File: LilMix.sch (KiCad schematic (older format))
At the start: 57 parts, among them J1_L1 MONO, J1_R1 MONO, J2_L1 MONO, J2_R1 MONO, J3 STEREO, J4 MONO, J5 MONO, J6 STEREO, U1 TL074, U2 NE5532

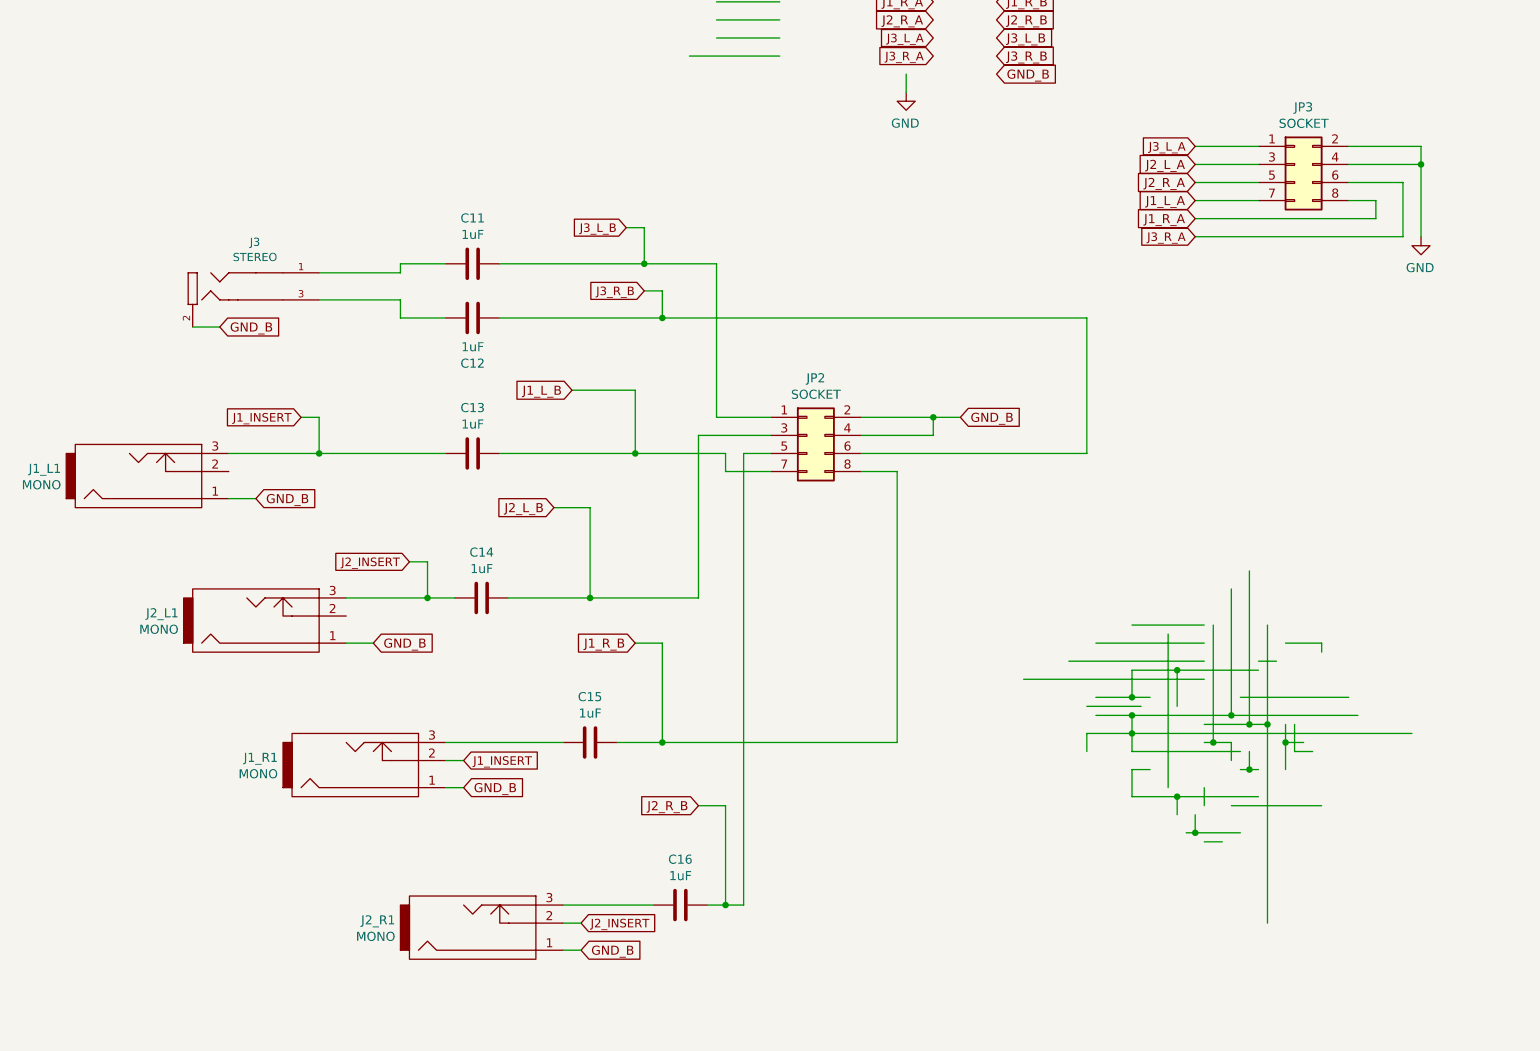
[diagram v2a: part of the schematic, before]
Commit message: Removed extra jack connection from schematic. Added second jack to 3rd channel. Repositioned jack board for even space between jacks, with slightly reduced overall dimensions
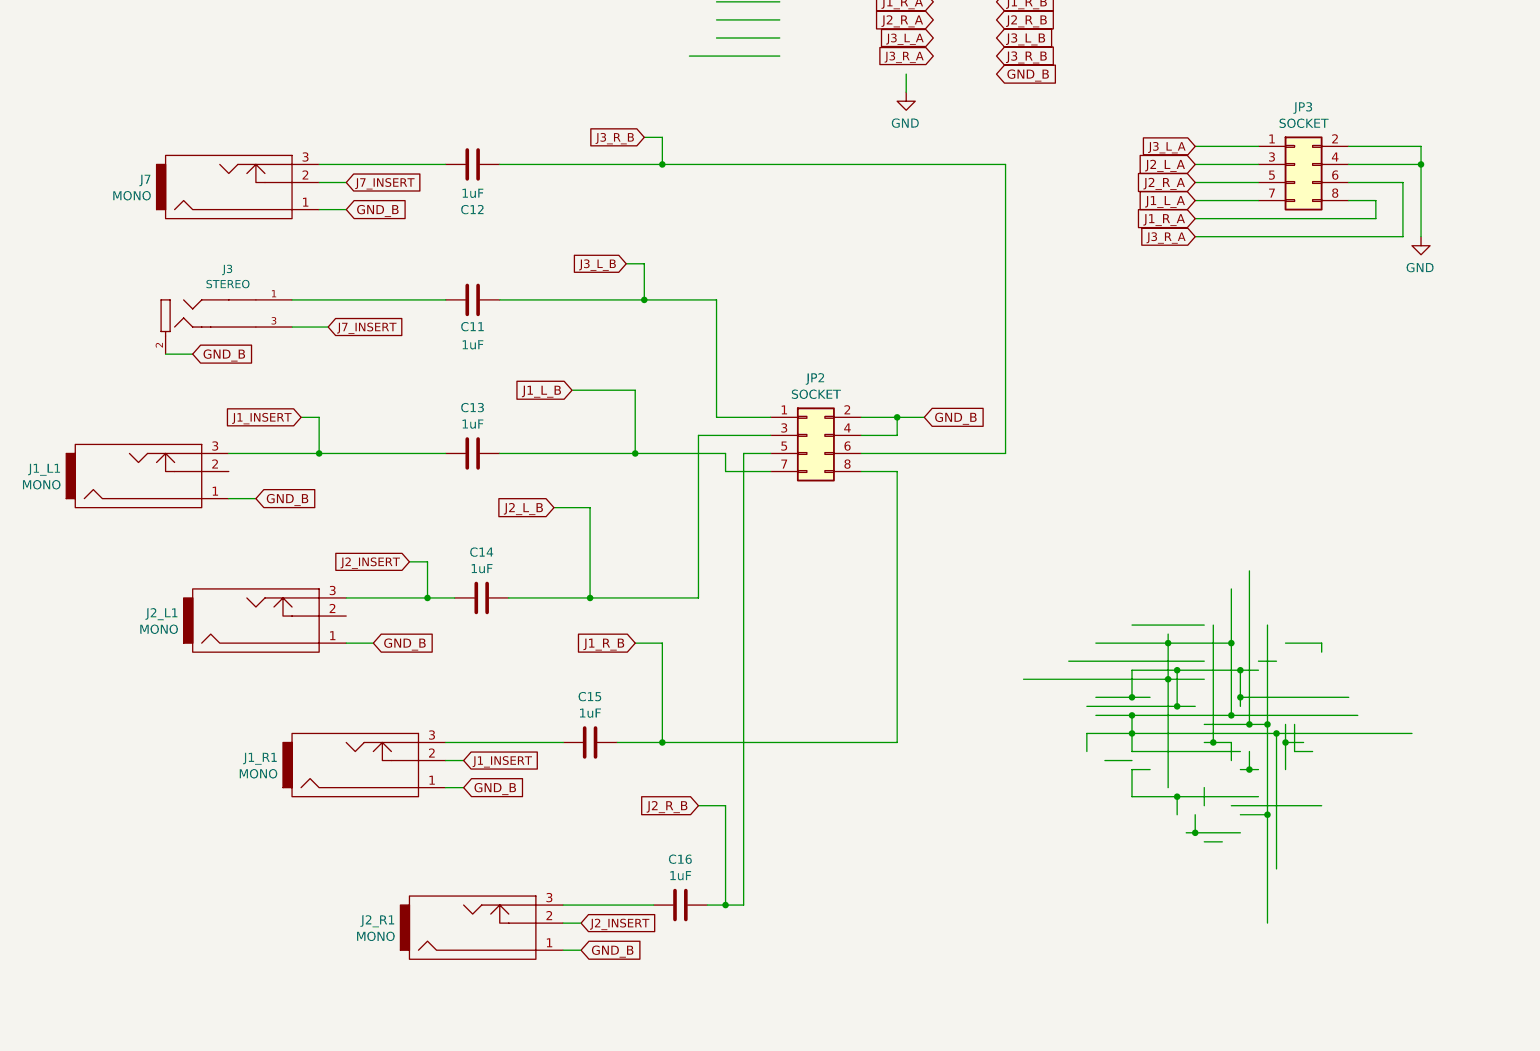
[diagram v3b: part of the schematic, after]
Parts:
- added J7: MONO, 4ms-footprints:PJ301M-12, symbol eurocad:PJ301M-12
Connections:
- net labels added: J7_INSERT
- wire segments 313 -> 326
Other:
- moved on the sheet: C11, C12, J3
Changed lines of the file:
@@
 EESchema Schematic File Version 4
-LIBS:LilMix-cache
 EELAYER 30 0
 EELAYER END
@@
 L 4ms-mech:JACK-STEREO-MINI J3
 U 1 1 5ECFAA7B
-P -6850 2450
-F 0 "J3" H -6905 2720 45  0000 C CNN
-F 1 "STEREO" H -6905 2636 45  0000 C CNN
-F 2 "Eurocad:STPX-3501-3C-1" H -6820 2600 20  0001 C CNN
-F 3 "" H -6850 2450 60  0001 C CNN
-	1    -6850 2450
+P -7000 2600
+F 0 "J3" H -7055 2870 45  0000 C CNN
+F 1 "STEREO" H -7055 2786 45  0000 C CNN
+F 2 "Eurocad:STPX-3501-3C-1" H -6970 2750 20  0001 C CNN
+F 3 "" H -7000 2600 60  0001 C CNN
+	1    -7000 2600
 	1    0    0    -1
 $EndComp
@@
 $EndComp
 Wire Wire Line
-	-4750 2100 -4850 2100
+	-4750 2300 -4850 2300
 Wire Wire Line
 	-5850 5050 -5750 5050
@@
 	0    1    -1   0
 $EndComp
-Text GLabel -4850 2100 0    47   Input ~ 0
+Text GLabel -4850 2300 0    47   Input ~ 0
 J3_L_B
 Text GLabel -5100 5950 2    47   Input ~ 0
@@
 	1000 2200 1450 2200
 Wire Wire Line
-	-2650 4600 -1650 4600
+	-2650 4600 -1850 4600
 Wire Wire Line
 	-6400 4400 -6250 4400
@@
 J2_R_B
 Wire Wire Line
-	-1850 4350 -1850 5200
-Wire Wire Line
-	-4650 2450 -4750 2450
-Text GLabel -4750 2450 0    47   Input ~ 0
+	-1850 4350 -1850 4400
+Wire Wire Line
+	-4650 1600 -4750 1600
+Text GLabel -4750 1600 0    47   Input ~ 0
 J3_R_B
 Text GLabel -2800 750  2    50   Input ~ 0
@@
 Wire Wire Line
 	1000 6000 1450 6000
-Text GLabel -3000 3150 2    50   Input ~ 0
+Text GLabel -3200 3150 2    50   Input ~ 0
 GND_B
 Wire Wire Line
-	-3150 3150 -3000 3150
+	-3350 3150 -3200 3150
 Text Notes -4050 7400 0    354  ~ 0
 LilMix External
@@
 Wire Wire Line
 	-2050 4300 -1650 4300
-Wire Wire Line
-	-1650 4400 -2250 4400
-Text GLabel -7100 2650 2    50   Input ~ 0
+Text GLabel -7250 2800 2    50   Input ~ 0
 GND_B
 Wire Wire Line
-	-7250 2650 -7100 2650
-Wire Wire Line
-	-3550 3250 -3150 3250
-Wire Wire Line
-	-3550 3150 -3150 3150
-Wire Wire Line
-	-3150 3150 -3150 3250
+	-7400 2800 -7250 2800
+Wire Wire Line
+	-3550 3250 -3350 3250
+Wire Wire Line
+	-3550 3150 -3350 3150
+Wire Wire Line
+	-3350 3150 -3350 3250
 Wire Wire Line
 	-7050 3350 -6550 3350
@@
 	1    0    0    -1
 $EndComp
-Connection ~ -3150 3150
+Connection ~ -3350 3150
 $Comp
 L 4ms-headers:Conn_02x04_Odd_Even JP3
@@
 L 4ms-passives:C C11
 U 1 1 5E6EE0E9
-P -5700 2300
-F 0 "C11" V -5952 2300 50  0000 C CNN
-F 1 "1uF" V -5861 2300 50  0000 C CNN
-F 2 "Capacitor_THT:C_Rect_L7.0mm_W4.5mm_P5.00mm" H -5662 2150 50  0001 C CNN
-F 3 "" H -5700 2300 50  0001 C CNN
-	1    -5700 2300
-	0    1    1    0
-$EndComp
-Wire Wire Line
-	-4650 2450 -4650 2600
+P -5700 2500
+F 0 "C11" V -5550 2500 50  0000 C CNN
+F 1 "1uF" V -5450 2500 50  0000 C CNN
+F 2 "Capacitor_THT:C_Rect_L7.0mm_W4.5mm_P5.00mm" H -5662 2350 50  0001 C CNN
+F 3 "" H -5700 2500 50  0001 C CNN
+	1    -5700 2500
+	0    1    1    0
+$EndComp
+Wire Wire Line
+	-4650 1600 -4650 1750
 $Comp
 L 4ms-passives:C C12
 U 1 1 5E77E136
-P -5700 2600
-F 0 "C12" V -5952 2600 50  0000 C CNN
-F 1 "1uF" V -5861 2600 50  0000 C CNN
-F 2 "Capacitor_THT:C_Rect_L7.0mm_W4.5mm_P5.00mm" H -5662 2450 50  0001 C CNN
-F 3 "" H -5700 2600 50  0001 C CNN
-	1    -5700 2600
+P -5700 1750
+F 0 "C12" V -5952 1750 50  0000 C CNN
+F 1 "1uF" V -5861 1750 50  0000 C CNN
+F 2 "Capacitor_THT:C_Rect_L7.0mm_W4.5mm_P5.00mm" H -5662 1600 50  0001 C CNN
+F 3 "" H -5700 1750 50  0001 C CNN
+	1    -5700 1750
 	0    -1   -1   0
 $EndComp
 Wire Wire Line
-	-6550 2350 -6100 2350
-Wire Wire Line
-	-6100 2350 -6100 2300
-Wire Wire Line
-	-6100 2300 -5850 2300
-Wire Wire Line
-	-5550 2300 -4750 2300
-Wire Wire Line
-	-4750 2300 -4750 2100
-Wire Wire Line
-	-2000 4750 -2300 4750
+	-5550 2500 -4750 2500
+Wire Wire Line
+	-4750 2500 -4750 2300
 Wire Wire Line
 	-1400 4000 -1400 4850
 Wire Wire Line
-	-6550 2500 -6100 2500
-Wire Wire Line
-	-6100 2500 -6100 2600
-Wire Wire Line
-	-6100 2600 -5850 2600
-Wire Wire Line
-	-5550 2600 -4650 2600
+	-5550 1750 -4650 1750
 Wire Wire Line
 	-1600 4300 -1600 4950
@@
 	-4050 3450 -4300 3450
 Wire Wire Line
-	-1500 4100 -1500 4800
+	-1500 4100 -1500 4400
 Wire Wire Line
 	-2250 4700 -2050 4700
@@
 	-4200 5850 -4300 5850
 Connection ~ -4300 5850
-Wire Wire Line
-	-4800 3350 -4300 3350
 Wire Wire Line
 	-4300 3350 -4300 3450
@@
 Connection ~ -5050 4150
 Wire Wire Line
-	-4650 2600 -2300 2600
-Wire Wire Line
-	-2300 2600 -2300 3350
-Wire Wire Line
-	-2300 3350 -3550 3350
-Connection ~ -4650 2600
+	-4650 1750 -2750 1750
+Wire Wire Line
+	-1250 4900 -1250 5650
+Connection ~ -4650 1750
 Wire Wire Line
 	-4050 3150 -4350 3150
 Wire Wire Line
-	-4350 3150 -4350 2300
-Wire Wire Line
-	-4350 2300 -4750 2300
-Connection ~ -4750 2300
+	-1850 4600 -1850 4400
+Wire Wire Line
+	-4350 2500 -4750 2500
+Connection ~ -4750 2500
 Connection ~ -2050 4700
 Connection ~ -2050 4800
 Connection ~ -1800 4550
 Wire Wire Line
-	-1800 4550 -1350 4550
+	-1800 4550 -1450 4550
 Wire Wire Line
 	-1450 4700 -850 4700
@@
 	-1400 5100 -1350 5100
 Wire Wire Line
-	-2050 4900 -500 4900
+	-2050 4900 -1250 4900
 Wire Wire Line
 	-2050 4800 -1500 4800
@@
 	-1000 4400 -1000 4450
 Wire Wire Line
-	-1300 4850 -1300 5950
+	-1300 4850 -1300 5350
 Connection ~ -1700 5450
 Wire Wire Line
@@
 Wire Wire Line
 	-1800 5250 -1350 5250
+$Comp
+L eurocad:PJ301M-12 J7
+U 1 1 5E5614B6
+P -7000 1850
+F 0 "J7" H -7478 1834 50  0000 R CNN
+F 1 "MONO" H -7478 1925 50  0000 R CNN
+F 2 "4ms-footprints:PJ301M-12" H -7000 1850 50  0001 C CNN
+F 3 "" H -7000 1850 50  0000 C CNN
+	1    -7000 1850
+	1    0    0    1
+$EndComp
+Wire Wire Line
+	-2750 3350 -2750 1750
+Wire Wire Line
+	-2050 5050 -2200 5050
+Connection ~ -1500 4400
+Connection ~ -1250 4900
+Wire Wire Line
+	-1250 4900 -500 4900
+Wire Wire Line
+	-2250 4400 -1850 4400
+Text GLabel -6400 1850 2    47   Input ~ 0
+J7_INSERT
+Wire Wire Line
+	-1450 4550 -1450 4700
+Wire Wire Line
+	-4350 3150 -4350 2500
+Connection ~ -1450 4550
+Wire Wire Line
+	-1450 4550 -1350 4550
+Connection ~ -1450 4700
+Wire Wire Line
+	-1450 4700 -1450 4750
+Wire Wire Line
+	-6700 2500 -5850 2500
+Wire Wire Line
+	-6550 1850 -6400 1850
+Text GLabel -6500 2650 2    47   Input ~ 0
+J7_INSERT
+Wire Wire Line
+	-6700 2650 -6500 2650
+Wire Wire Line
+	-6550 1750 -5850 1750
+Connection ~ -1800 4750
+Wire Wire Line
+	-1800 4750 -1700 4750
+Wire Wire Line
+	-2300 4750 -1800 4750
+Wire Wire Line
+	-1500 4400 -1500 4800
+Wire Wire Line
+	-1450 5350 -1300 5350
+Wire Wire Line
+	-2750 3350 -3550 3350
+Connection ~ -1300 5350
+Wire Wire Line
+	-1300 5350 -1300 5950
+Text GLabel -6400 2000 2    50   Input ~ 0
+GND_B
+Wire Wire Line
+	-6550 2000 -6400 2000
+Connection ~ -1850 4400
+Wire Wire Line
+	-1850 4400 -1500 4400
+Connection ~ -1850 4600
+Wire Wire Line
+	-1850 4600 -1650 4600
+Wire Wire Line
+	-1850 4600 -1850 5200
+Wire Wire Line
+	-4800 3350 -4300 3350
 $EndSCHEMATC

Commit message: Fixed J7 insert
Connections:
- wire segments 326 -> 325
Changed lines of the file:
@@
 J2_INSERT
 Wire Wire Line
-	-6550 3150 -6550 3350
-Wire Wire Line
-	-6650 3150 -6550 3150
-Text GLabel -6650 3150 0    47   Input ~ 0
+	-6900 3450 -7050 3450
+Text GLabel -6900 3450 2    47   Input ~ 0
 J1_INSERT
 Wire Wire Line
@@
 Wire Wire Line
 	-3350 3150 -3350 3250
-Wire Wire Line
-	-7050 3350 -6550 3350
 $Comp
 L 4ms-headers:Conn_02x04_Odd_Even JP2
@@
 Wire Wire Line
 	-4800 3350 -5550 3350
-Wire Wire Line
-	-5850 3350 -6550 3350
-Connection ~ -6550 3350
 $Comp
 L 4ms-passives:C C14
@@
 	-1400 5100 -1350 5100
 Wire Wire Line
-	-2050 4900 -1250 4900
-Wire Wire Line
 	-2050 4800 -1500 4800
 Wire Wire Line
@@
 	-1850 4600 -1650 4600
 Wire Wire Line
+	-4800 3350 -4300 3350
+Wire Wire Line
+	-7050 3350 -5850 3350
+Wire Wire Line
 	-1850 4600 -1850 5200
 Wire Wire Line
-	-4800 3350 -4300 3350
+	-2050 4900 -1250 4900
+Wire Wire Line
+	-1750 4950 -1750 5150
 $EndSCHEMATC

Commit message: Change TL074 output channel feedback resistors, based on BB results
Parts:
- R11, R12, R15, R16: value 10k -> 100k
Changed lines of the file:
@@
 P 7550 1150
 F 0 "R15" V 7650 1150 50  0000 C CNN
-F 1 "10k" V 7434 1150 50  0000 C CNN
+F 1 "100k" V 7434 1150 50  0000 C CNN
 F 2 "Resistor_SMD:R_0805_2012Metric_Pad1.15x1.40mm_HandSolder" V 7480 1150 50  0001 C CNN
 F 3 "" H 7550 1150 50  0001 C CNN
@@
 P 7550 2750
 F 0 "R16" V 7650 2750 50  0000 C CNN
-F 1 "10k" V 7434 2750 50  0000 C CNN
+F 1 "100k" V 7434 2750 50  0000 C CNN
 F 2 "Resistor_SMD:R_0805_2012Metric_Pad1.15x1.40mm_HandSolder" V 7480 2750 50  0001 C CNN
 F 3 "" H 7550 2750 50  0001 C CNN
@@
 P 6900 3100
 F 0 "R12" V 7000 3100 50  0000 C CNN
-F 1 "10k" V 6784 3100 50  0000 C CNN
+F 1 "100k" V 6784 3100 50  0000 C CNN
 F 2 "Resistor_SMD:R_0805_2012Metric_Pad1.15x1.40mm_HandSolder" V 6830 3100 50  0001 C CNN
 F 3 "" H 6900 3100 50  0001 C CNN
@@
 P 6900 1500
 F 0 "R11" V 7000 1500 50  0000 C CNN
-F 1 "10k" V 6784 1500 50  0000 C CNN
+F 1 "100k" V 6784 1500 50  0000 C CNN
 F 2 "Resistor_SMD:R_0805_2012Metric_Pad1.15x1.40mm_HandSolder" V 6830 1500 50  0001 C CNN
 F 3 "" H 6900 1500 50  0001 C CNN

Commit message: Fix J1 insert from T rather than S
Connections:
- wire segments 325 -> 327
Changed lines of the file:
@@
 J2_INSERT
 Wire Wire Line
-	-6900 3450 -7050 3450
-Text GLabel -6900 3450 2    47   Input ~ 0
+	-6300 3150 -6150 3150
+Text GLabel -6300 3150 0    47   Input ~ 0
 J1_INSERT
 Wire Wire Line
@@
 Wire Wire Line
 	-1800 5250 -1350 5250
+Wire Wire Line
+	-2750 3350 -2750 1750
+Wire Wire Line
+	-2050 5050 -2200 5050
+Connection ~ -1500 4400
+Connection ~ -1250 4900
+Wire Wire Line
+	-1250 4900 -500 4900
+Wire Wire Line
+	-2250 4400 -1850 4400
+Wire Wire Line
+	-1450 4550 -1450 4700
+Wire Wire Line
+	-4350 3150 -4350 2500
+Connection ~ -1450 4550
+Wire Wire Line
+	-1450 4550 -1350 4550
+Connection ~ -1450 4700
+Wire Wire Line
+	-1450 4700 -1450 4750
+Wire Wire Line
+	-6700 2500 -5850 2500
+Connection ~ -1800 4750
+Wire Wire Line
+	-1800 4750 -1700 4750
+Wire Wire Line
+	-2300 4750 -1800 4750
+Wire Wire Line
+	-1500 4400 -1500 4800
+Wire Wire Line
+	-1450 5350 -1300 5350
+Wire Wire Line
+	-2750 3350 -3550 3350
+Connection ~ -1300 5350
+Wire Wire Line
+	-1300 5350 -1300 5950
+Connection ~ -1850 4400
+Wire Wire Line
+	-1850 4400 -1500 4400
+Connection ~ -1850 4600
+Wire Wire Line
+	-1850 4600 -1650 4600
+Wire Wire Line
+	-4800 3350 -4300 3350
+Wire Wire Line
+	-7050 3350 -6150 3350
+Wire Wire Line
+	-1850 4600 -1850 5200
+Wire Wire Line
+	-2050 4900 -1250 4900
+Wire Wire Line
+	-1750 4950 -1750 5150
+Wire Wire Line
+	-6700 2650 -6500 2650
+Text GLabel -6500 2650 2    47   Input ~ 0
+J7_INSERT
+Wire Wire Line
+	-6550 2000 -6400 2000
+Text GLabel -6400 2000 2    50   Input ~ 0
+GND_B
+Wire Wire Line
+	-6550 1750 -5850 1750
+Wire Wire Line
+	-6550 1850 -6400 1850
+Text GLabel -6400 1850 2    47   Input ~ 0
+J7_INSERT
 $Comp
 L eurocad:PJ301M-12 J7
@@
 $EndComp
 Wire Wire Line
-	-2750 3350 -2750 1750
-Wire Wire Line
-	-2050 5050 -2200 5050
-Connection ~ -1500 4400
-Connection ~ -1250 4900
-Wire Wire Line
-	-1250 4900 -500 4900
-Wire Wire Line
-	-2250 4400 -1850 4400
-Text GLabel -6400 1850 2    47   Input ~ 0
-J7_INSERT
-Wire Wire Line
-	-1450 4550 -1450 4700
-Wire Wire Line
-	-4350 3150 -4350 2500
-Connection ~ -1450 4550
-Wire Wire Line
-	-1450 4550 -1350 4550
-Connection ~ -1450 4700
-Wire Wire Line
-	-1450 4700 -1450 4750
-Wire Wire Line
-	-6700 2500 -5850 2500
-Wire Wire Line
-	-6550 1850 -6400 1850
-Text GLabel -6500 2650 2    47   Input ~ 0
-J7_INSERT
-Wire Wire Line
-	-6700 2650 -6500 2650
-Wire Wire Line
-	-6550 1750 -5850 1750
-Connection ~ -1800 4750
-Wire Wire Line
-	-1800 4750 -1700 4750
-Wire Wire Line
-	-2300 4750 -1800 4750
-Wire Wire Line
-	-1500 4400 -1500 4800
-Wire Wire Line
-	-1450 5350 -1300 5350
-Wire Wire Line
-	-2750 3350 -3550 3350
-Connection ~ -1300 5350
-Wire Wire Line
-	-1300 5350 -1300 5950
-Text GLabel -6400 2000 2    50   Input ~ 0
-GND_B
-Wire Wire Line
-	-6550 2000 -6400 2000
-Connection ~ -1850 4400
-Wire Wire Line
-	-1850 4400 -1500 4400
-Connection ~ -1850 4600
-Wire Wire Line
-	-1850 4600 -1650 4600
-Wire Wire Line
-	-4800 3350 -4300 3350
-Wire Wire Line
-	-7050 3350 -5850 3350
-Wire Wire Line
-	-1850 4600 -1850 5200
-Wire Wire Line
-	-2050 4900 -1250 4900
-Wire Wire Line
-	-1750 4950 -1750 5150
+	-6150 3150 -6150 3350
+Connection ~ -6150 3350
+Wire Wire Line
+	-6150 3350 -5850 3350
 $EndSCHEMATC
